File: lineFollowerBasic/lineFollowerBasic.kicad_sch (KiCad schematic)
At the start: 7 parts, among them J1 Conn_01x0_Pin, SW1 SW_Push, U1 ATmega328-P, Y1 16MHz Crystal

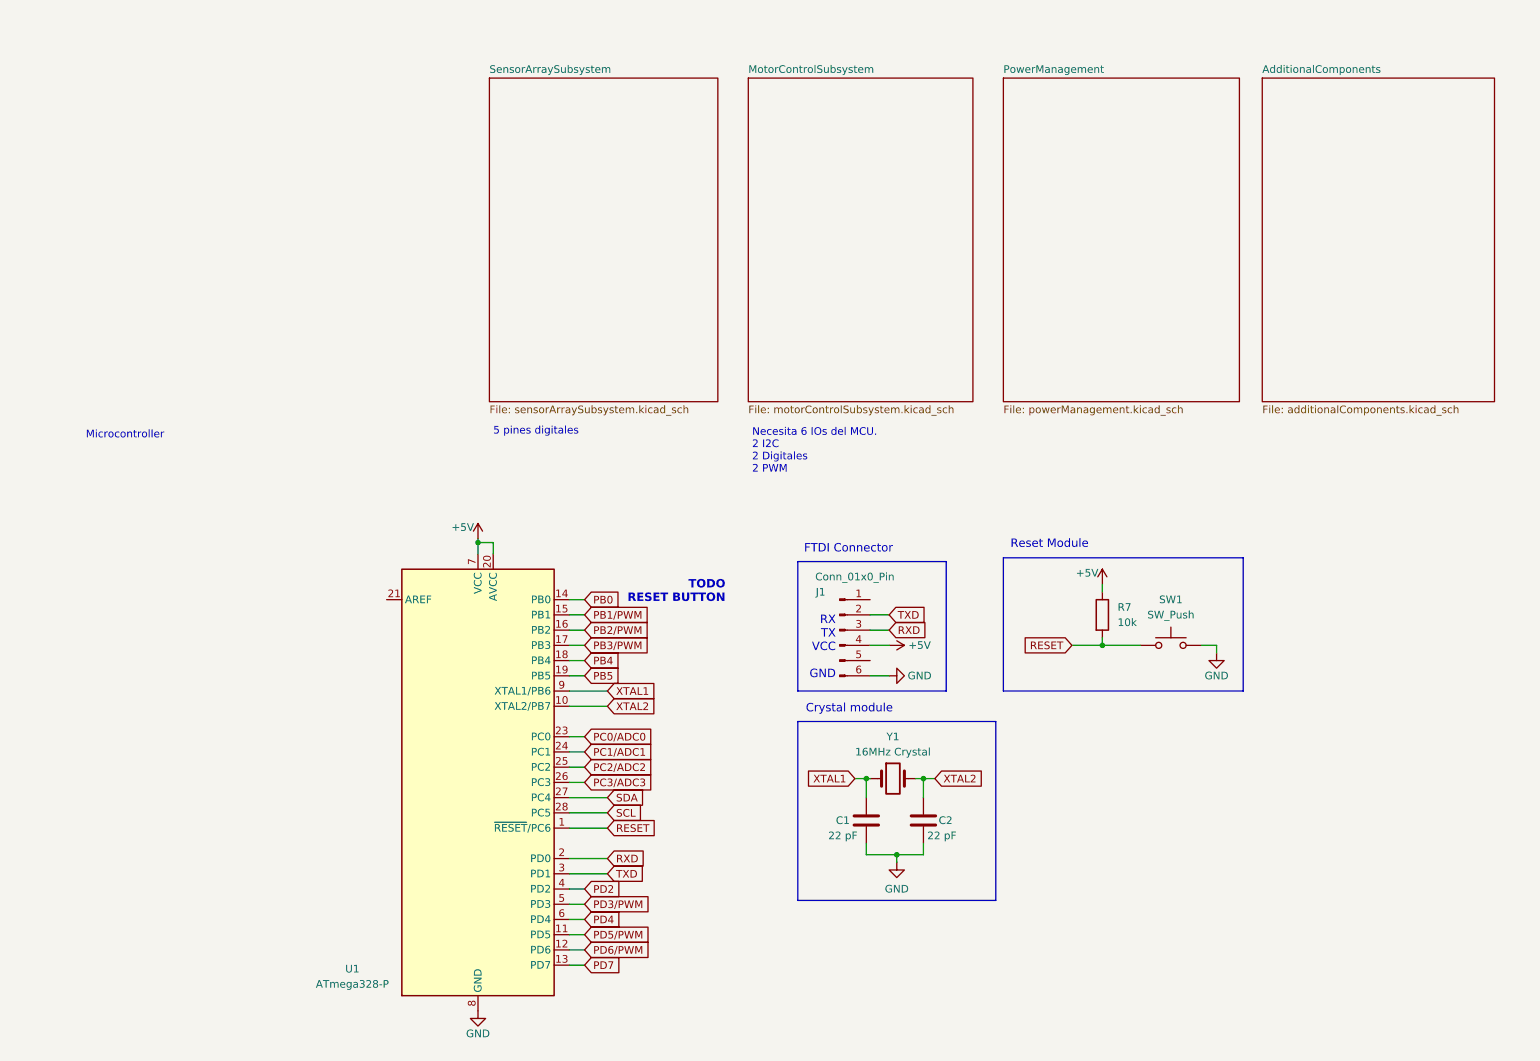
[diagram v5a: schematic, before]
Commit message: Added LEDs, and UI switches, TODO: assign labels and DIP circuit
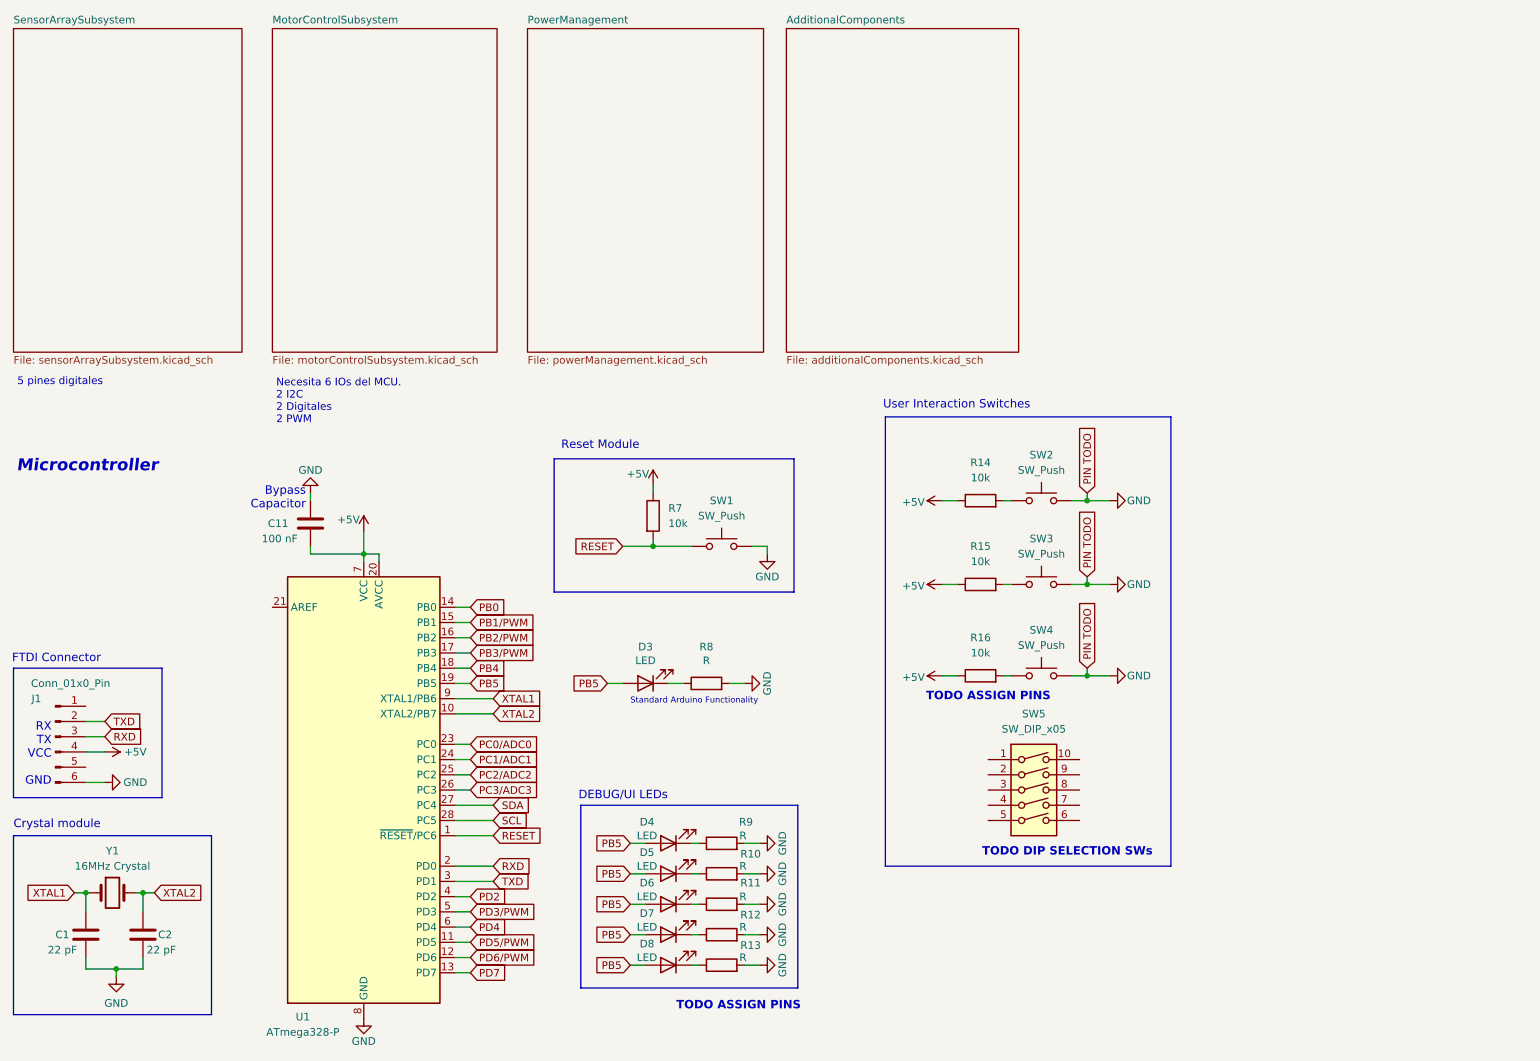
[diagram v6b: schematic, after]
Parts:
- added C11: 100 nF, symbol Device:C
- added D3, D4, D5, D6, D7, D8: LED, symbol Device:LED
- added R10, R11, R12, R13, R8, R9: R, symbol Device:R
- added R14, R15, R16: 10k, symbol Device:R
- added SW2, SW3, SW4: SW_Push, symbol Switch:SW_Push
- added SW5: SW_DIP_x05, symbol Switch:SW_DIP_x05
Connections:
- net +5V: now also C11.2, R14.1, R15.1, R16.1
- net GND: now also C11.1, R10.2, R11.2, R12.2, R13.2, R8.2, R9.2, SW2.2, SW3.2, SW4.2
- net PB5: now also D3.2 (A), D4.2 (A), D5.2 (A), D6.2 (A), D7.2 (A), D8.2 (A)
- new net: R15.2, SW3.1
- new net: D8.1 (K), R13.1
- new net: R14.2, SW2.1
- new net: D3.1 (K), R8.1
- new net: D5.1 (K), R10.1
- new net: D4.1 (K), R9.1
- new net: D6.1 (K), R11.1
- new net: R16.2, SW4.1
- new net: D7.1 (K), R12.1
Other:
- note added: "Bypass Capacitor"
- note added: "DEBUG/UI LEDs"
- note added: "Standard Arduino Functionality"
- note added: "TODO ASSIGN PINS"
- note added: "TODO DIP SELECTION SWs"
- note added: "User Interaction Switches"
- note removed: "TODO RESET BUTTON"
- moved on the sheet: C1, C2, J1, R7, SW1, U1, Y1
